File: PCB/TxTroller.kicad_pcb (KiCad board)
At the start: 2 copper layers, 19.9 x 34 mm, 8 parts, among them J1 RadioReceiver, Q1 2N2222, U1 XIAO-RP2040-DIP

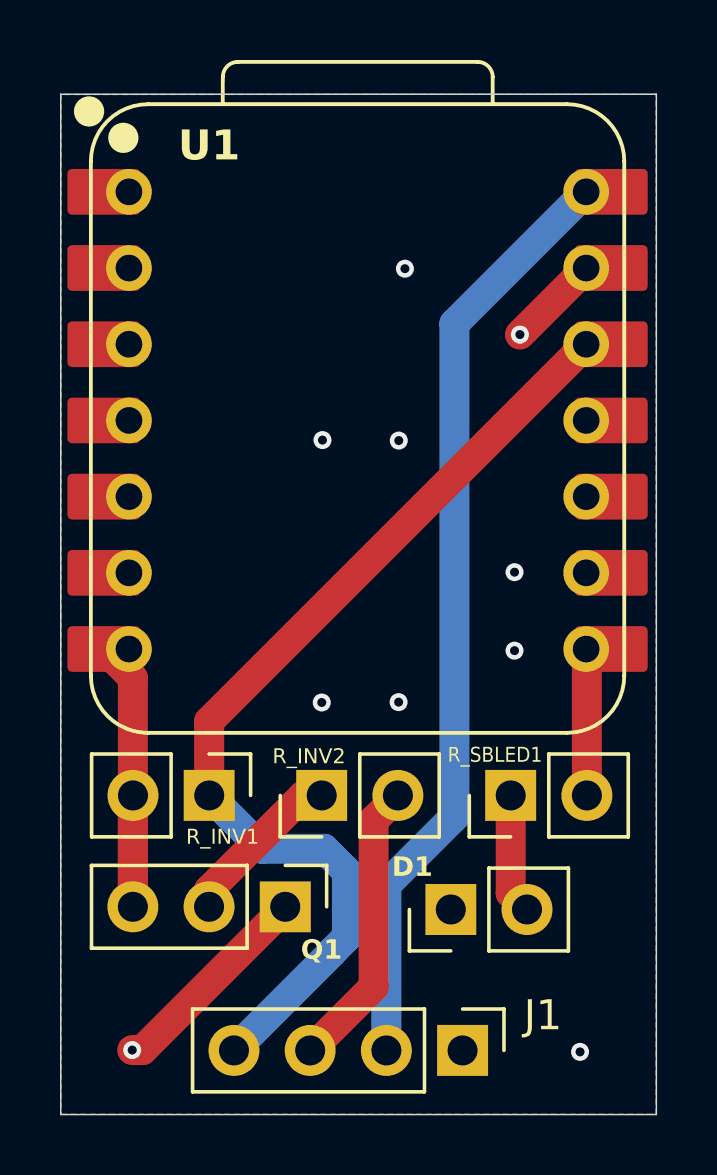
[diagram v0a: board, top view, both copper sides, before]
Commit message: fixed pin assignments
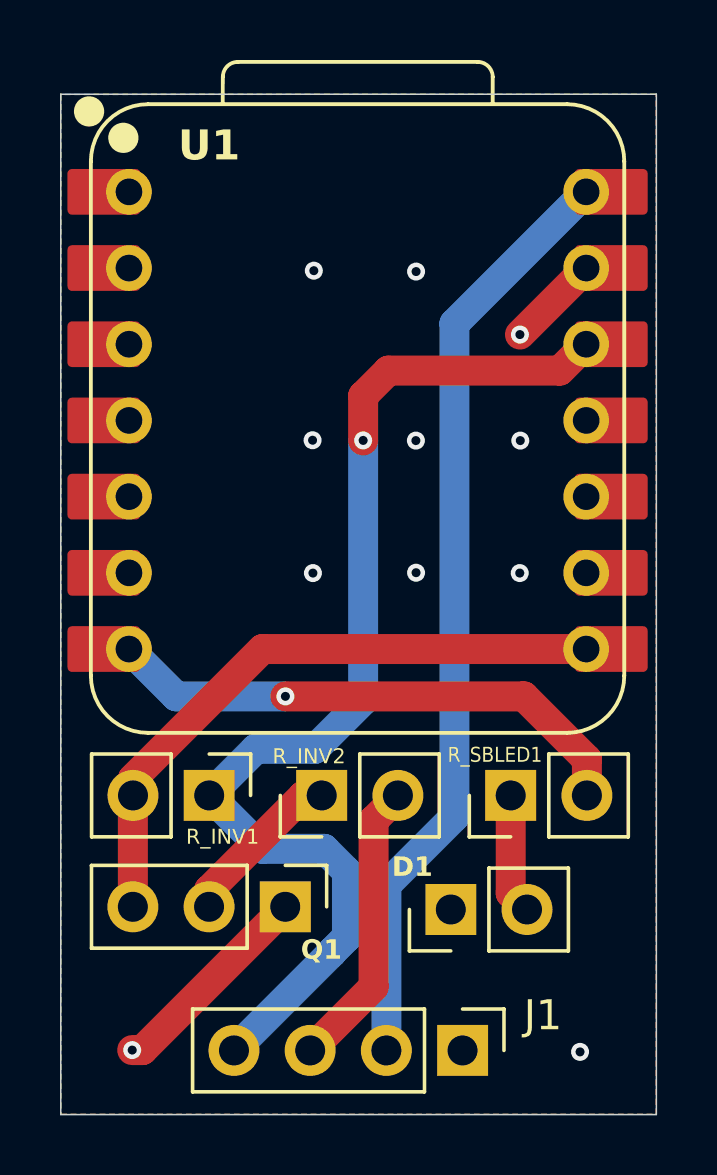
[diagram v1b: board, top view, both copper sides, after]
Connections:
- U1 pad 7: /<NO NET> -> /SBUS_STAT
- U1 pad 8: /SBUS_STAT -> /<NO NET>
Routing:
- net /SBUS_STAT: track 4.89 -> 18.0 mm, vias 0 -> 1
- net /<NO NET>: track 12.7 -> 21.2 mm
- net +3V3: track 33.4 -> 37.9 mm, vias 0 -> 1
- net GND: vias 10 -> 11
